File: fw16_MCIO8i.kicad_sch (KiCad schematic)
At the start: 13 parts

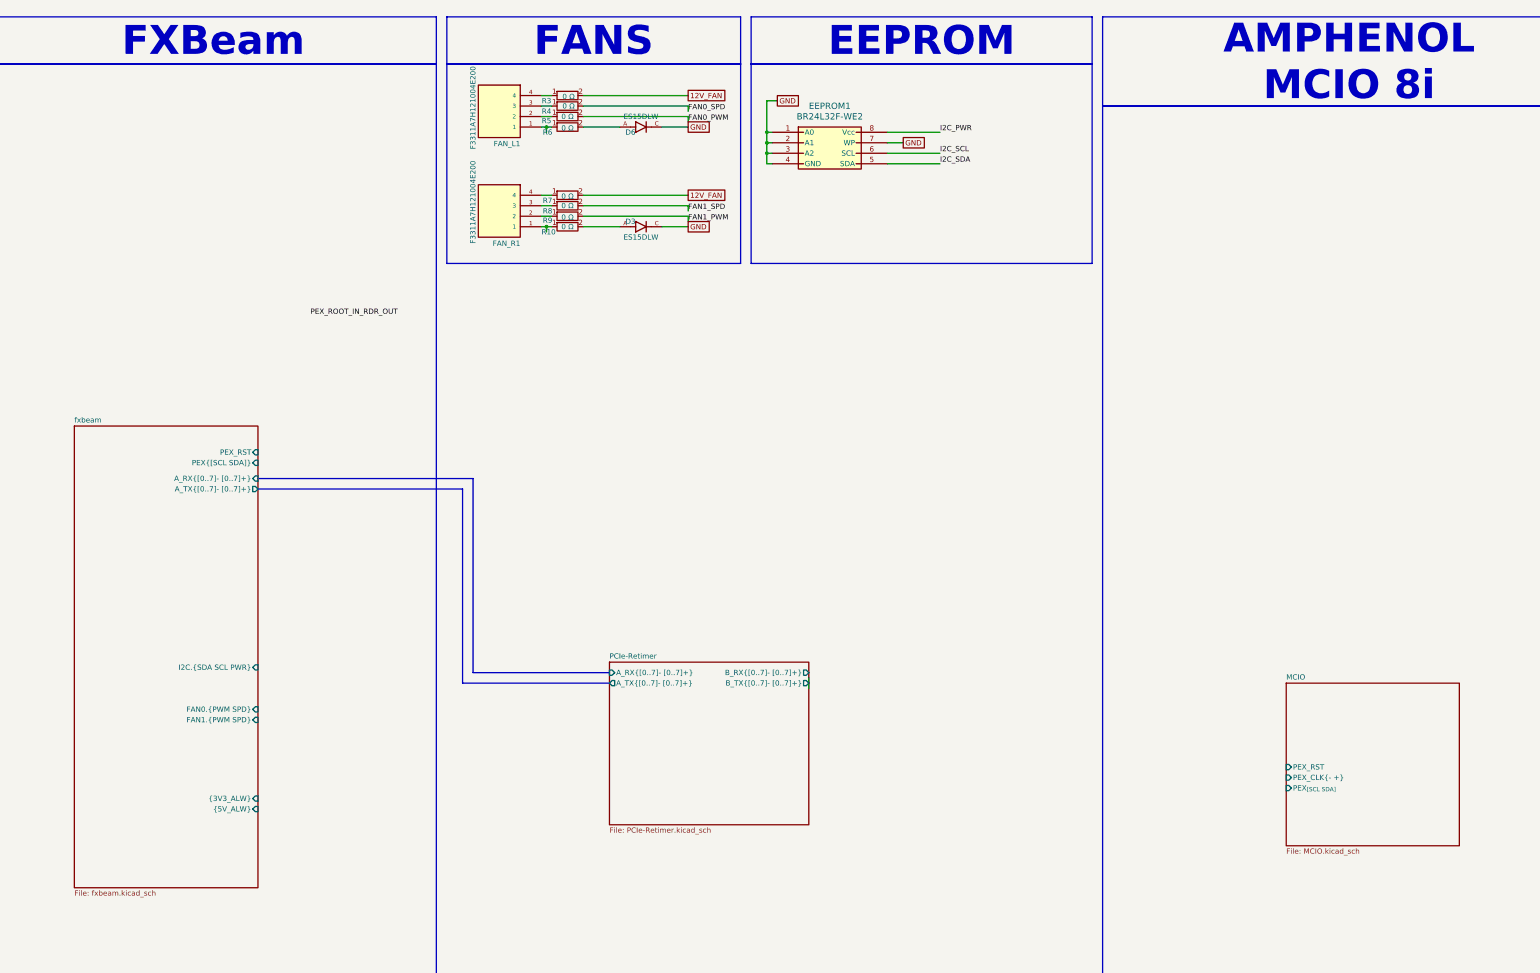
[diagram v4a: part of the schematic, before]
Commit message: moved schematics
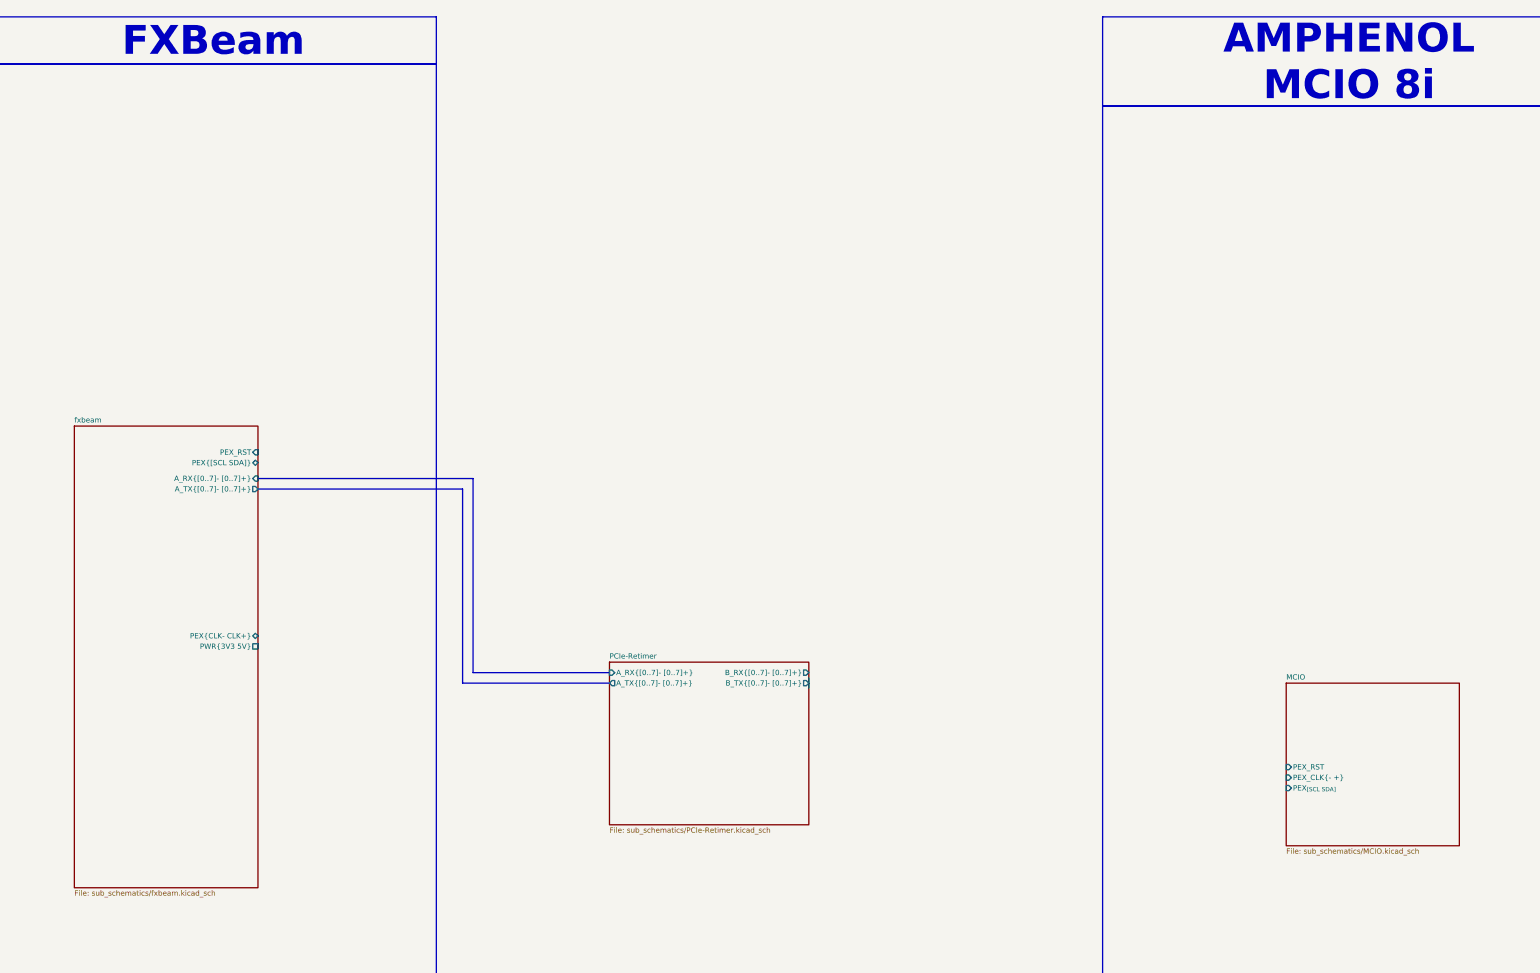
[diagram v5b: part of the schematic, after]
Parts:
- removed D3, D6: ES15DLW, fan-diode:SODFL3718X102N, symbol fan-diode:ES15DLW
- removed EEPROM1: BR24L32F-WE2, eeprom:SOP8_ROM, symbol eeprom:BR24L32F-WE2
- removed FAN_L1, FAN_R1: F3311A7H121004E200, fan-connector:AMPHENOL_F3311A7H121004E200, symbol fan-connector:F3311A7H121004E200
- removed R10, R3, R4, R5, R6, R7, R8, R9: 1206_R_560112132007, resistors:R_Wurth_WRIS-RSKS-1206_R, symbol resistor:1206_R_560112132007
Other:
- sheet MCIO: file MCIO.kicad_sch -> sub_schematics/MCIO.kicad_sch
- sheet PCIe-Retimer: file PCIe-Retimer.kicad_sch -> sub_schematics/PCIe-Retimer.kicad_sch
- sheet fxbeam: file fxbeam.kicad_sch -> sub_schematics/fxbeam.kicad_sch
- sheet fxbeam ports: added PEX{CLK- CLK+}, PWR{3V3 5V}; removed FAN0.{PWM SPD}, FAN1.{PWM SPD}, I2C.{SDA SCL PWR}, {3V3_ALW}, {5V_ALW}

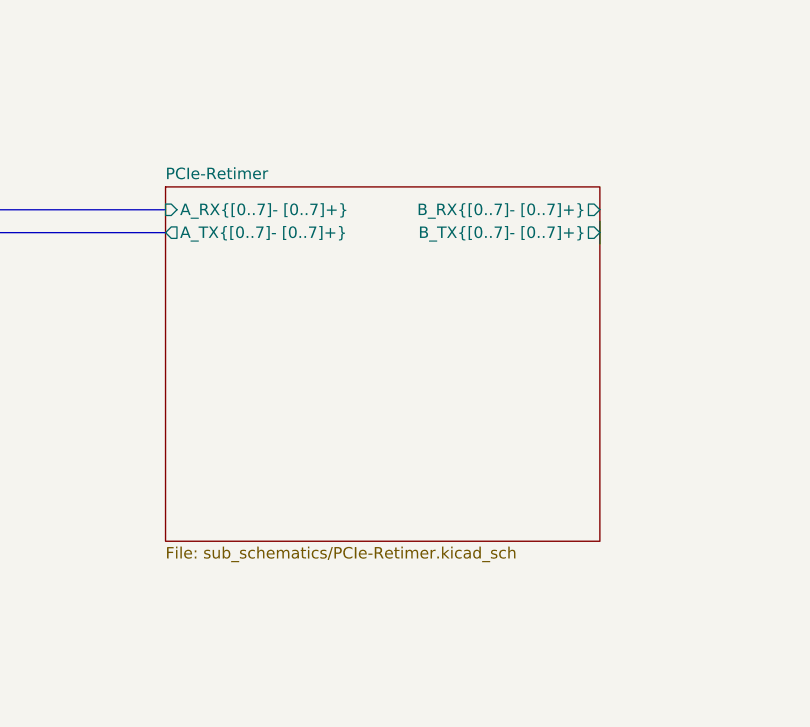
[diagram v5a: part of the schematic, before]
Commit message: buck converter changes
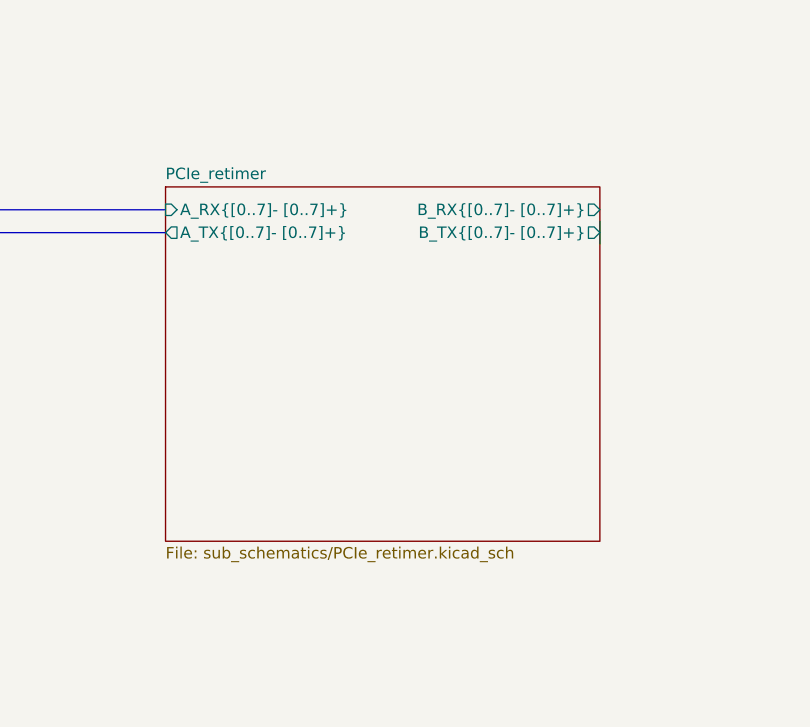
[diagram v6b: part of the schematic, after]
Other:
- sheet PCIe-Retimer renamed PCIe_retimer
- sheet PCIe_retimer: file sub_schematics/PCIe-Retimer.kicad_sch -> sub_schematics/PCIe_retimer.kicad_sch
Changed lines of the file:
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@@
 			(color 0 0 0 0)
 		)
-		(property "Sheetname" "PCIe-Retimer"
+		(property "Sheetname" "PCIe_retimer"
 			(at 166.37 172.0084 0)
 			(show_name no)
@@
 			)
 		)
-		(property "Sheetfile" "sub_schematics/PCIe-Retimer.kicad_sch"
+		(property "Sheetfile" "sub_schematics/PCIe_retimer.kicad_sch"
 			(at 166.37 212.6746 0)
 			(show_name no)

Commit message: buck converter
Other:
- sheet PCIe_retimer ports: added PWR{3V3 5V}; removed none
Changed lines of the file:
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@@
+	(bus
+		(pts
+			(xy 110.49 189.23) (xy 166.37 189.23)
+		)
+		(stroke
+			(width 0)
+			(type default)
+		)
+	)
 	(bus
 		(pts
@@
 	(bus
 		(pts
+			(xy 110.49 166.37) (xy 110.49 189.23)
+		)
+		(stroke
+			(width 0)
+			(type default)
+		)
+	)
+	(bus
+		(pts
 			(xy 81.28 128.27) (xy 133.35 128.27)
 		)
@@
 		(pts
 			(xy 214.63 176.53) (xy 214.63 179.07)
+		)
+		(stroke
+			(width 0)
+			(type default)
+		)
+	)
+	(bus
+		(pts
+			(xy 81.28 166.37) (xy 110.49 166.37)
 		)
 		(stroke
@@
 			)
 		)
+		(pin "PWR{3V3 5V}" passive
+			(at 166.37 189.23 180)
+			(effects
+				(font
+					(size 1.27 1.27)
+				)
+				(justify left)
+			)
+		)

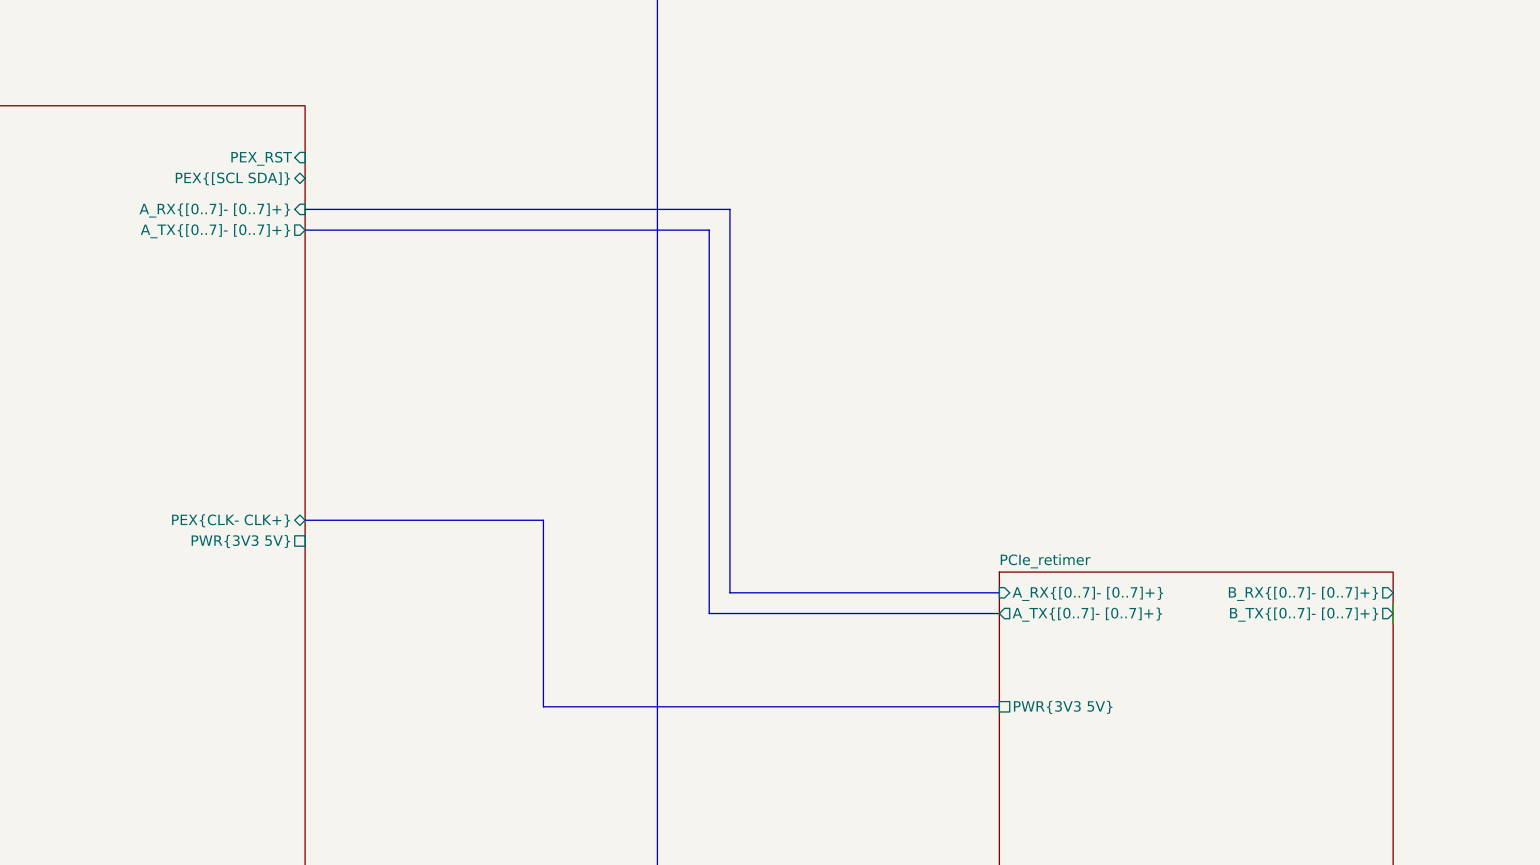
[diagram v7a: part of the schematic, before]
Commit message: Schematics revamped
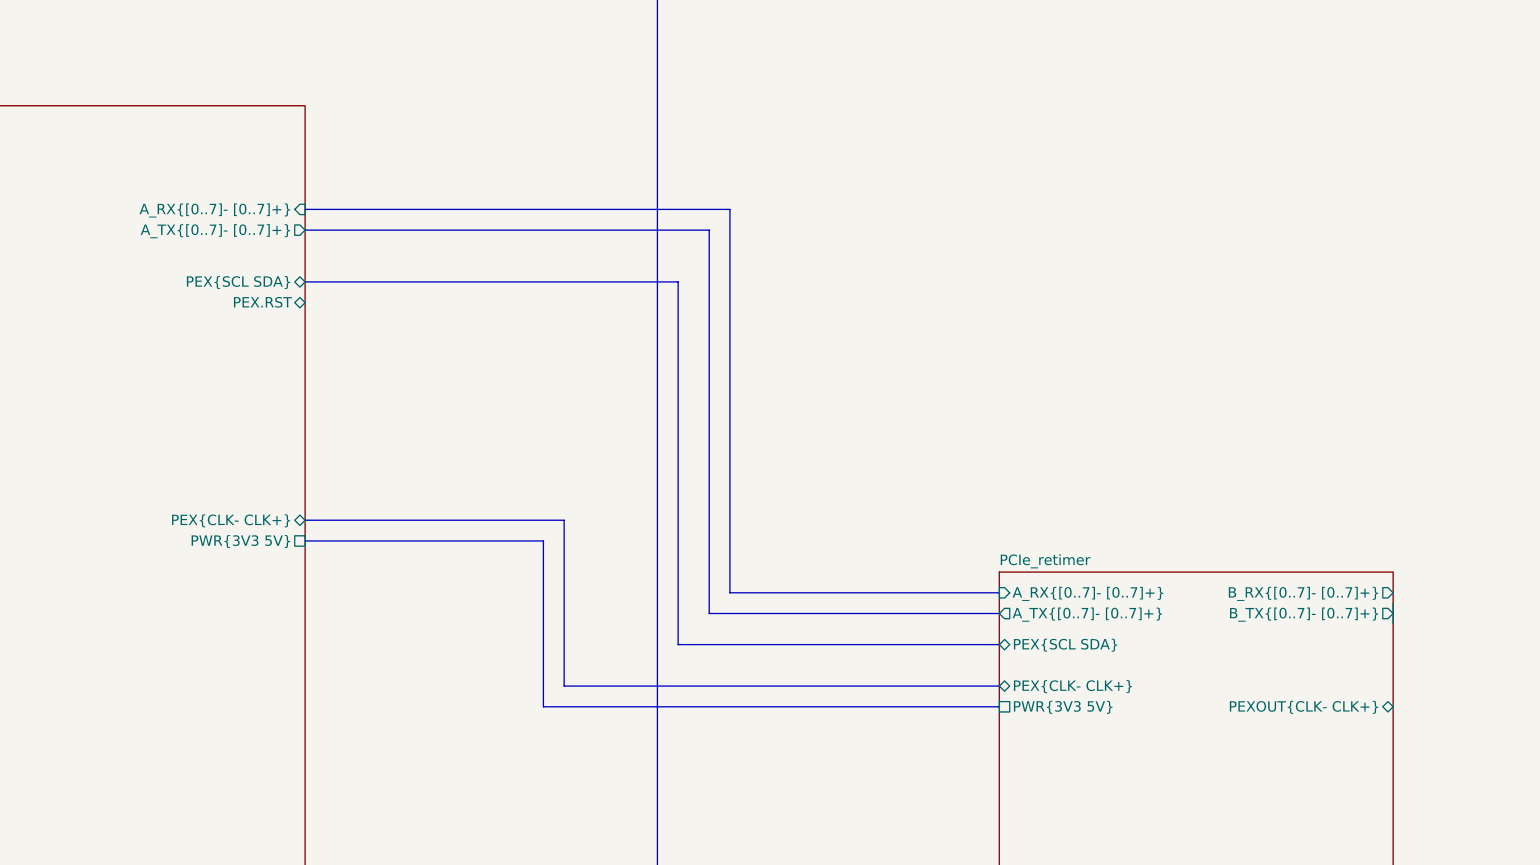
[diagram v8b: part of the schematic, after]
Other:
- sheet PCIe_retimer ports: added PEXOUT{CLK- CLK+}, PEX{CLK- CLK+}, PEX{SCL SDA}; removed none
- sheet fxbeam ports: added PEX.RST, PEX{SCL SDA}; removed PEX_RST, PEX{[SCL SDA]}
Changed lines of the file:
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@@
+	(bus
+		(pts
+			(xy 81.28 168.91) (xy 110.49 168.91)
+		)
+		(stroke
+			(width 0)
+			(type default)
+		)
+	)
+	(bus
+		(pts
+			(xy 110.49 168.91) (xy 110.49 189.23)
+		)
+		(stroke
+			(width 0)
+			(type default)
+		)
+	)
 	(bus
 		(pts
@@
 	(bus
 		(pts
+			(xy 113.03 186.69) (xy 166.37 186.69)
+		)
+		(stroke
+			(width 0)
+			(type default)
+		)
+	)
+	(bus
+		(pts
 			(xy 130.81 130.81) (xy 130.81 177.8)
 		)
@@
 	(bus
 		(pts
+			(xy 127 137.16) (xy 127 181.61)
+		)
+		(stroke
+			(width 0)
+			(type default)
+		)
+	)
+	(bus
+		(pts
+			(xy 81.28 137.16) (xy 127 137.16)
+		)
+		(stroke
+			(width 0)
+			(type default)
+		)
+	)
+	(bus
+		(pts
 			(xy 133.35 128.27) (xy 133.35 175.26)
 		)
@@
 	(bus
 		(pts
-			(xy 110.49 166.37) (xy 110.49 189.23)
-		)
-		(stroke
-			(width 0)
-			(type default)
-		)
-	)
-	(bus
-		(pts
 			(xy 81.28 128.27) (xy 133.35 128.27)
 		)
@@
 	(bus
 		(pts
+			(xy 127 181.61) (xy 166.37 181.61)
+		)
+		(stroke
+			(width 0)
+			(type default)
+		)
+	)
+	(bus
+		(pts
 			(xy 130.81 177.8) (xy 166.37 177.8)
 		)
@@
 	(bus
 		(pts
-			(xy 81.28 166.37) (xy 110.49 166.37)
+			(xy 81.28 166.37) (xy 113.03 166.37)
+		)
+		(stroke
+			(width 0)
+			(type default)
+		)
+	)
+	(bus
+		(pts
+			(xy 113.03 166.37) (xy 113.03 186.69)
 		)
 		(stroke
@@
 			(project "fw16_MCIO8i"
 				(path "/50f5fd03-67f8-43d1-8bfe-dca2cf908bf0"
-					(page "3")
+					(page "4")
 				)
 			)
@@
 			)
 		)
-		(pin "PEX_RST" input
-			(at 81.28 121.92 0)
-			(effects
-				(font
-					(size 1.27 1.27)
-				)
-				(justify right)
-			)
-		)
-		(pin "PEX{[SCL SDA]}" bidirectional
-			(at 81.28 124.46 0)
-			(effects
-				(font
-					(size 1.27 1.27)
-				)
-				(justify right)
-			)
-		)
 		(pin "A_TX{[0..7]- [0..7]+}" output
 			(at 81.28 130.81 0)
@@
 		(pin "PWR{3V3 5V}" passive
 			(at 81.28 168.91 0)
+			(effects
+				(font
+					(size 1.27 1.27)
+				)
+				(justify right)
+			)
+		)
+		(pin "PEX.RST" bidirectional
+			(at 81.28 139.7 0)
+			(effects
+				(font
+					(size 1.27 1.27)
+				)
+				(justify right)
+			)
+		)
+		(pin "PEX{SCL SDA}" bidirectional
+			(at 81.28 137.16 0)
 			(effects
 				(font
@@
 			(effects
 				(font
+					(size 1.27 1.27)
+				)
+				(justify left)
+			)
+		)
+		(pin "PEXOUT{CLK- CLK+}" bidirectional
+			(at 214.63 189.23 0)
+			(effects
+				(font
+					(size 1.27 1.27)
+				)
+				(justify right)
+			)
+		)
+		(pin "PEX{CLK- CLK+}" bidirectional
+			(at 166.37 186.69 180)
+			(effects
+				(font
+					(size 1.27 1.27)
+				)
+				(justify left)
+			)
+		)
+		(pin "PEX{SCL SDA}" bidirectional
+			(at 166.37 181.61 180)
+			(effects
+				(font
